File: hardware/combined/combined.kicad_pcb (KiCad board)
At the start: 2 copper layers, 62 x 208.5 mm, 143 parts, among them J1 USB-C 5V in, J2 Mini-DIN-8 to printer, J4 Mini-DIN-8 LocalTalk, SW1 EVQP44B3M, SW2 B3U-1000P, SW3 TS-1002-BR16026, U1 ESP32-S3-WROOM-1-N8R2, U2 SP3490EN-L, U3 SP3232EEN, U4 AP7361C-33E, U5 USBLC6-2SC6, U6 SP3485EN-L, U7 PIC12F1840-I/P, U8 SP3485EN-L, U9 74AHCT1G125SE-7

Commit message: SW1: redraw EVQP44B3M footprint from Panasonic ANCTB27E, move to the east edge
The old footprint was an admitted estimate: four pads at (+-2.55, +-1.0). The real
part has two contacts at +-2.275 mm, 2.05-3.1 mm from the board edge, and two
anchor tabs at +-3.2 mm, 0.45-1.25 mm from the edge. Each contact fell between
two old pads and each tab overlapped one, so EN would have bonded to a frame tab.
New footprint traced from the drawing (tabs un-netted); SW1 placed so the push
plate is flush with x=162; EN rerouted; GND via added. DRC 0/0 with parity.
Combined file, fab package and render regenerated.
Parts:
- moved SW1 2.33 mm to (160.3, 99.5)
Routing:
- net /EN: track 56.1 -> 57.7 mm
- net /GND: track 0.00 -> 1.40 mm, vias 43 -> 44

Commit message: LEDs: drop the pad-1 silk labels; keep Wells's inboard SW1 position; antenna copper stays
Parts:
- moved SW1 3.05 mm to (157.2, 99.5)
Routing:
- net /EN: track 57.7 -> 52.4 mm
- net /GND: track 1.40 -> 0.00 mm

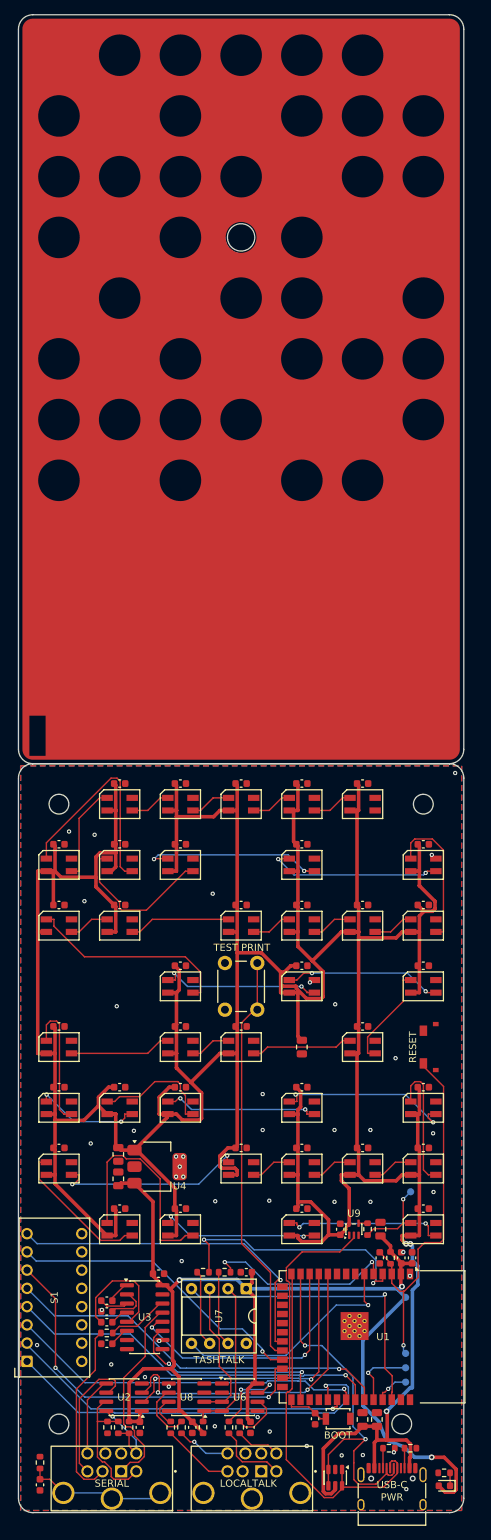
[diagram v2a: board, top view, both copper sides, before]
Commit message: Panel: plate the test hole — gold to the bore, no black surround
The 3.8mm test hole becomes a plated pad (O4.4 pad, copper layers only):
the bore wall takes ENIG and reads gold, the keep_dia black surround and
its sub-0.1mm mask sliver are gone, and mask opens to the drill edge.
Pad + annulus ring + tab art share decorative net PANEL_AU so their
contact doesn't DRC as a short; combine_boards.py carries that one net
through and strips all others (a pad's stripped (net 0) doesn't parse -
delete the node instead). Flood window grown to clear the pad by 0.25mm.
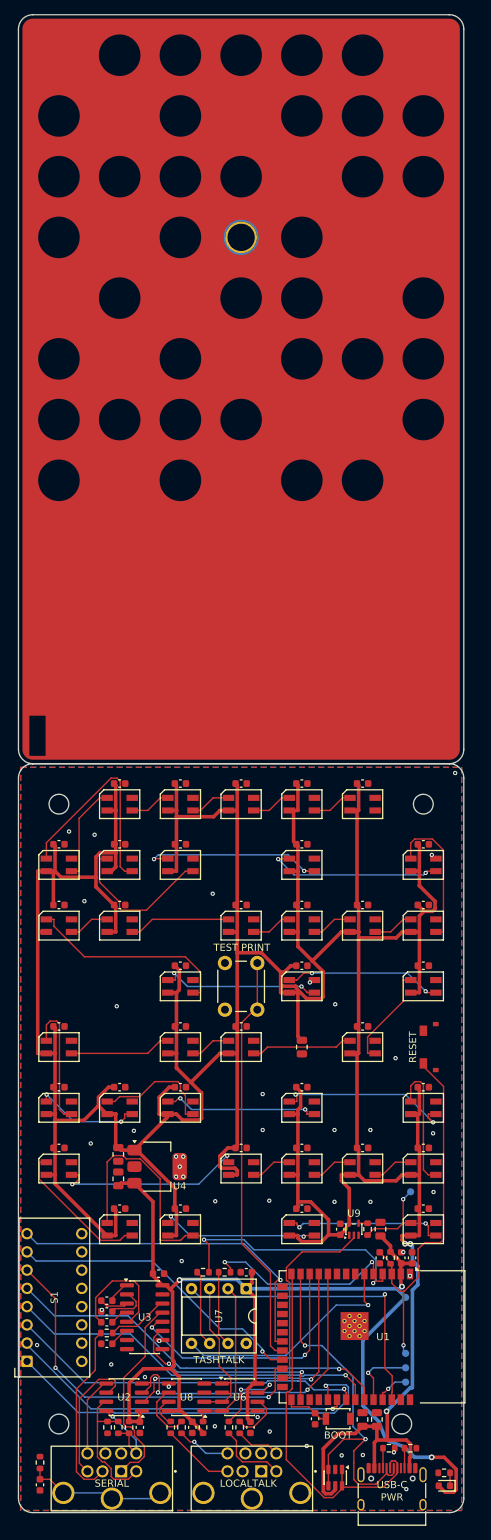
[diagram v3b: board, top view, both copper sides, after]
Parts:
- moved MT3 100.1 mm to (156.4, 47.7)
- moved MT4 98.6 mm to (108.6, 47.7)
- moved MT2 86.3 mm to (105.6, -38.6)
- moved MT1 86.3 mm to (156.4, -38.6)
- renumbered MT3 to MT1, MT4 to MT2, MT2 to MT3, MT1 to MT4
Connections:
- H_TEST pad : (no net) -> PANEL_AU

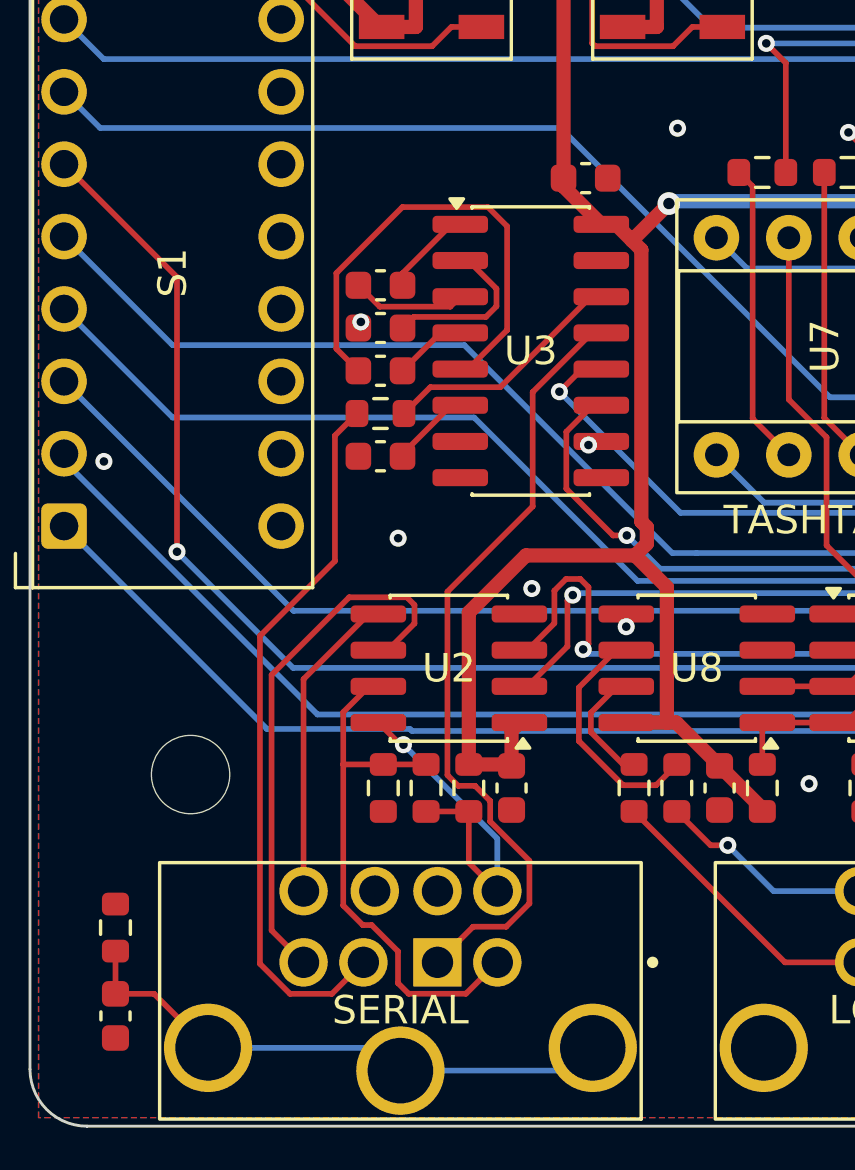
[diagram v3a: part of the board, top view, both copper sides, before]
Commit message: Review #4 fixes: J2 flipped to Mac-style, THT thermal reliefs, D3 restocked part, order notes corrected
Fourth adversarial pre-order review (layout, LCSC parts, circuit); report in
docs/review-2026-09-01-pre-order-4.md. No dead-on-arrival defect found; these are the
fixes it produced:

- J2 (printer port) is now wired as a Macintosh serial port so Apple's own crossover
  cable (590-0552-A / M0197) is the right cable. Schematic labels swapped 1<->2, 3<->5,
  6<->8; six nets hand re-routed (three new signal vias, one GND stitch via at
  111.45,152.6); DNP resistors R5 and R7 rotated 180 deg to suit the new pin map.
  J2 and J4 now read the same way.
- Both /GND zones use THT thermal reliefs (were solid; J2/J4 are hand-soldered).
  The change stranded one island, re-tied by tools_pcb/r12_fix.py with a via at
  119.626,131.048. GND is one cluster, 153/153 pads.
- D3 is LCSC C12624 (KT-0603G); C72043 had one unit in stock.
- ORDER-NOTES: 0.12 mm (4.7 mil) space exception around U4's tab (the .kicad_dru
  always required it), corrected via-fill answer (13 vias touch SMD pads, four fully
  inside U3.10/C9.2/C12.2/U1.1), D3 part, and the printer-cable guidance.
- Combined package regenerated (pos 127 rows, drill floor 0.30, 3.8 mm PTH, seam
  copper >= 0.5 mm) and the assembly render refreshed.
- Docs: SPEC 2.4 rewritten for the Mac-style J2 and the cable; HANDOFF entry with the
  bring-up traps (LT_DE floats as shipped, IO35/T1IN float, never ICSP the PIC in the
  socket, IO48 brownout loop) and drift corrections (LED caps at 2.87 mm, SW1 on the
  east edge, H4 coordinates, J4 shell direct to GND); firmware audit corrected on IO35.

Verification: ERC 0 errors; source DRC --severity-all --schematic-parity
--refill-zones = 0 errors / 0 unconnected (5 lib notes, 80 field-parity notes);
combined-file DRC baseline unchanged apart from one benign starved_thermal on U7.8.
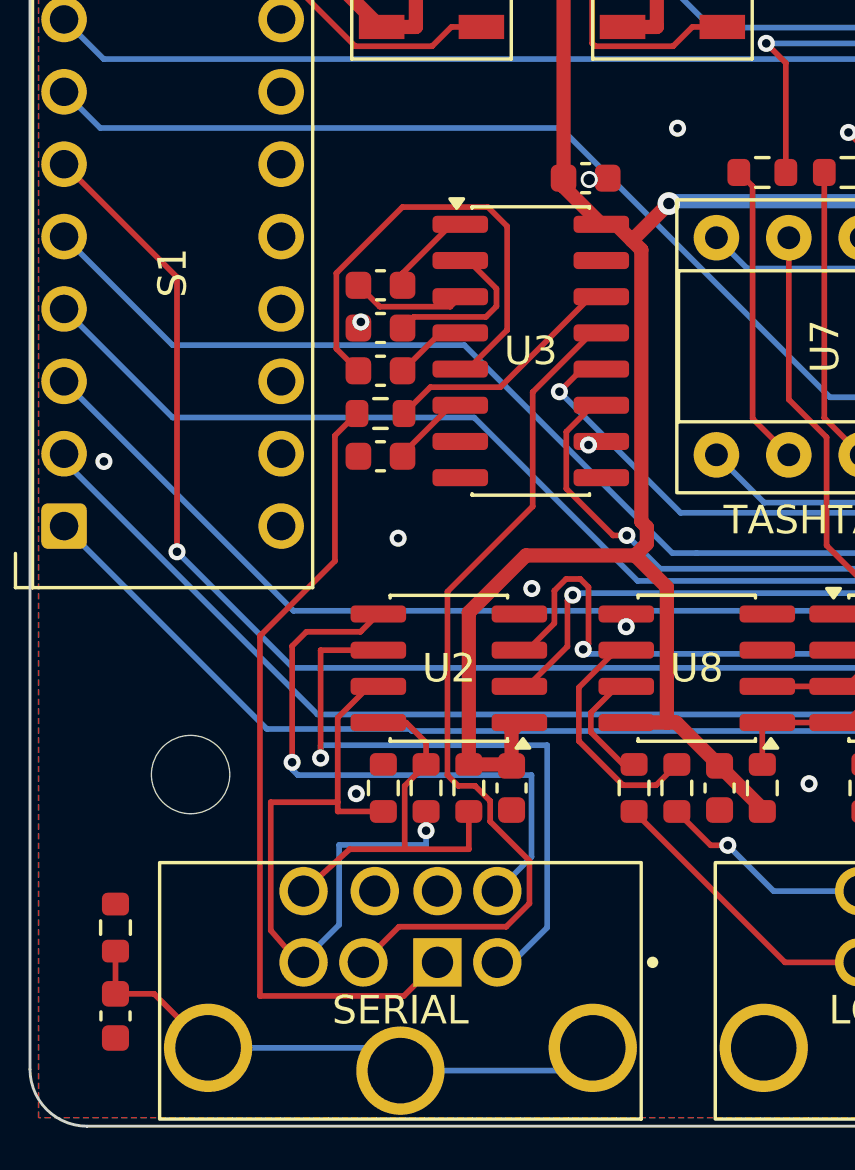
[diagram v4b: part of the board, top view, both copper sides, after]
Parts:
- turned R5 to -90 degrees
- turned R7 to 90 degrees
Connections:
- J2 pad 1: /PR_HSKO -> /PR_HSKI
- J2 pad 2: /PR_HSKI -> /PR_HSKO
- J2 pad 3: /PR_TXD_N -> /PR_RXD_N
- J2 pad 5: /PR_RXD_N -> /PR_TXD_N
- J2 pad 6: /PR_TXD_P -> /PR_RXD_P
- J2 pad 8: /PR_RXD_P -> /PR_TXD_P
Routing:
- net /PR_RXD_P: track 11.0 -> 20.9 mm, vias 0 -> 1
- net /PR_TXD_N: track 19.1 -> 24.1 mm, vias 0 -> 1
- net /PR_RXD_N: track 19.1 -> 22.9 mm, vias 0 -> 1
- net /PR_HSKI: track 25.2 -> 28.6 mm
- net /PR_HSKO: track 28.1 -> 30.7 mm
- net /PR_TXD_P: track 12.4 -> 13.7 mm, vias 1 -> 0
- net /GND: vias 44 -> 46

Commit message: Panel: swap too-small test label for a dot mark (PCBWay EQ)
PCBWay flagged the "test" soldermask label on the cover panel as below
their minimum feature size. Frame 9 drops that four-glyph label and adds a
~0.9mm accent dot in the test cell's lobe, with the lobe corner radius
opened from 10u to 12u.

The dot is emitted as a #111111 mask-knockout path -- the panel pipeline
ignores <circle> and only ingests white/#fff/#111 fills, so a plain black
circle would have been silently dropped. As a knockout it renders as a
kept-soldermask island on exposed gold. Regenerated panel -> combined ->
fab. Smallest B_Mask features in that cell: 0.90mm island, 0.23mm opening.
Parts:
- moved MT2 100.1 mm to (105.6, -38.6)
- moved MT3 100.1 mm to (156.4, 47.7)
- renumbered MT3 to MT2, MT2 to MT3

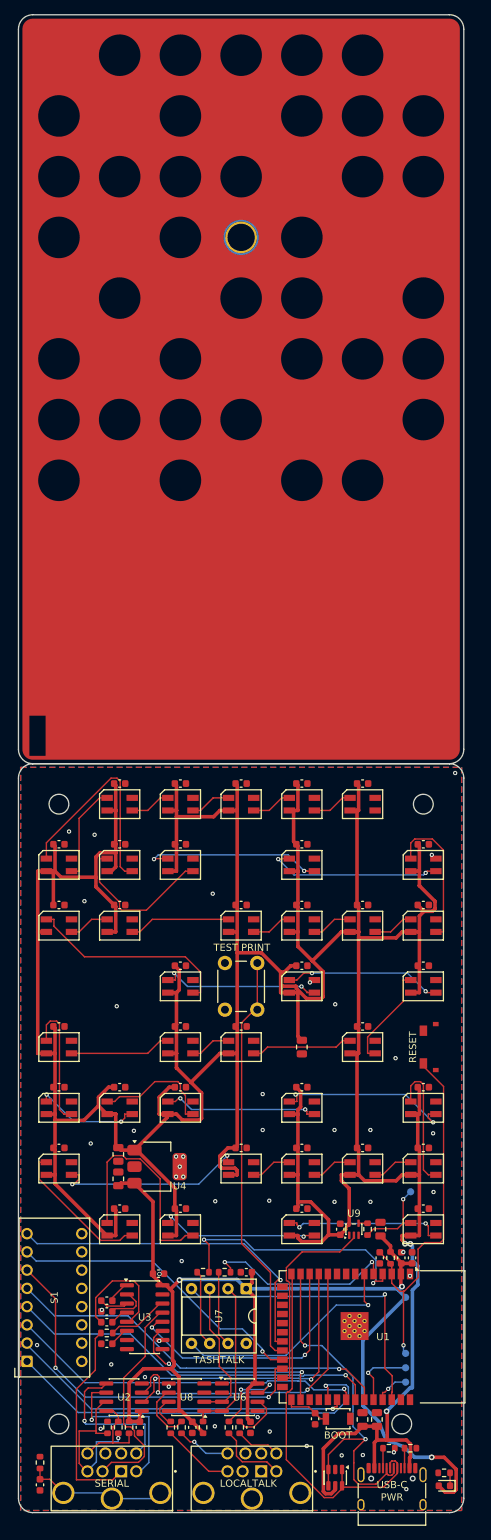
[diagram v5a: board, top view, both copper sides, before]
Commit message: Fab package: regenerated from the routed rev 2026.11 board (W-1091)
138 placements on AirWriter, 61 on Lite; drill floor 0.30 mm. The combined
panel's DRC under its default rules shows only the known kinds; R17 and D3 add
one copper-edge and one silk-edge item each way, both clear under the main
board's own 0.25 mm edge rule.
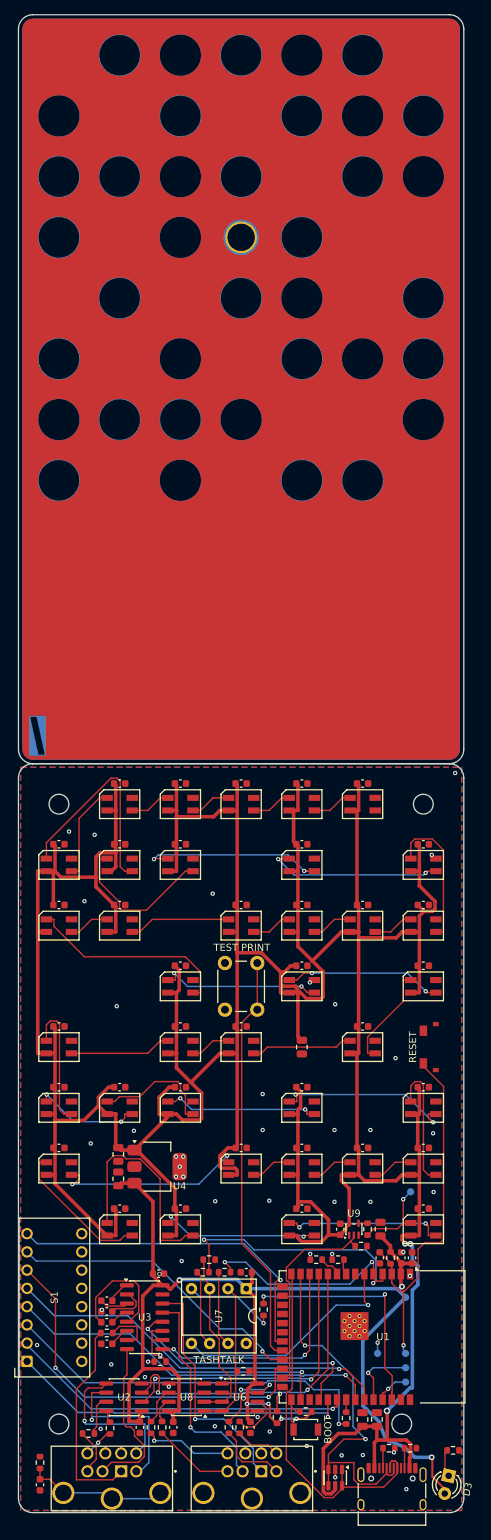
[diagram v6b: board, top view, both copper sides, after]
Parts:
- removed C7: 100n, Capacitor_SMD:C_0603_1608Metric
- removed R5: 120R, Resistor_SMD:R_0603_1608Metric
- removed R6, R7: 4.7k, Resistor_SMD:R_0603_1608Metric
- added R21: 10k, Resistor_SMD:R_0603_1608Metric, F.Cu at (140.0, 150.2)
- added R22: 10k, Resistor_SMD:R_0603_1608Metric, F.Cu at (126.5, 129.1)
- added R23: 10k, Resistor_SMD:R_0603_1608Metric, F.Cu at (147.7, 127.2)
- added R24: 10k, Resistor_SMD:R_0603_1608Metric, F.Cu at (119.7, 143.2)
- added R25: 10k, Resistor_SMD:R_0603_1608Metric, F.Cu at (136.0, 151.0)
- added R27: 1k, Resistor_SMD:R_0603_1608Metric, F.Cu at (134.1, 136.0)
- added R28: 1k, Resistor_SMD:R_0603_1608Metric, F.Cu at (145.6, 151.1)
- added R29: 10k, Resistor_SMD:R_0603_1608Metric, F.Cu at (112.8, 152.5)
- added R30: 10k, Resistor_SMD:R_0603_1608Metric, F.Cu at (109.8, 153.2)
- added R32: 10k, Resistor_SMD:R_0603_1608Metric, F.Cu at (141.4, 129.1)
- added R33: 10k, Resistor_SMD:R_0603_1608Metric, F.Cu at (144.5, 129.1)
- added TP9: GND, TestPoint_Pad_D1.0mm, B.Cu at (150.0, 142.1)
- D3: footprint LED_SMD:LED_0603_1608Metric -> airwriter:LED_D3.0mm_Spacer_H8mm
- R17: value 1k -> 150R
- SW3: value TS-1002-BR16026 -> TS-1002-BR15026
- U3: value SP3232EEN -> SP3232EBEN-L/TR
- U9: value 74AHCT1G125SE-7 -> SN74LV1T125DCKR
- moved R14 9.60 mm to (131.3, 144.6), turned to 180 degrees
- moved SW2 4.74 mm to (140.0, 152.7)
- moved R11 4.25 mm to (118.5, 152.4)
- moved R17 3.37 mm to (160.5, 155.6), turned to 0 degrees
- moved C18 2.65 mm to (121.5, 152.4)
- moved D3 1.51 mm to (159.9, 159.1), turned to -102.5 degrees
- moved R10 1.20 mm to (120.0, 152.4)
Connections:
- net /LT_A renamed /LT_RXD_N
- net /LT_B renamed /LT_RXD_P
- net /LT_PORT_A renamed /LT_PORT_RXD_N
- net /LT_PORT_B renamed /LT_PORT_RXD_P
- net /LT_PORT_Y renamed /LT_PORT_TXD_N
- net /LT_PORT_Z renamed /LT_PORT_TXD_P
- net /LT_Y renamed /LT_TXD_N
- net /LT_Z renamed /LT_TXD_P
- J4 pad 1: unconnected-(J4-HSKo-Pad1) -> /J4_HSKO
- J4 pad 2: unconnected-(J4-HSKi-Pad2) -> /J4_HSKI
- U1 pad 30: unconnected-(U1-IO37-Pad30) -> /J4_HSKI_RX
- U1 pad 33: /DIP3 -> /DIP3_GPIO
- U1 pad 8: unconnected-(U1-IO15-Pad8) -> /BOARD_LITE
- U1 pad 9: unconnected-(U1-IO16-Pad9) -> /BOARD_REV
- U2 pad 7: /PR_TXD_N -> /PR_TXD_N_IN
- U2 pad 8: /PR_TXD_P -> /PR_TXD_P_IN
- U3 pad 10: /GND -> /HSKI_DRV
- U3 pad 12: /UART_CTS -> /J4_HSKI_RX
- U3 pad 13: /PR_HSKO -> /J4_HSKI
- U3 pad 14: /HSKI_RS232 -> /J4_HSKO
- U3 pad 7: unconnected-(U3-T2OUT-Pad7) -> /HSKI_RS232
- U3 pad 8: /GND -> /PR_HSKO
- U3 pad 9: unconnected-(U3-R2OUT-Pad9) -> /UART_CTS
- U7 pad 4: /LT_RESET -> /LT_MCLR
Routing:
- net /J4_HSKI_RX: track 0.00 -> 35.4 mm, vias 0 -> 2
- net /J4_HSKO: track 0.00 -> 33.1 mm, vias 0 -> 1
- net /J4_HSKI: track 0.00 -> 30.2 mm, vias 0 -> 1
- net /PR_TXD_N: track 24.1 -> 6.47 mm, vias 1 -> 0
- net /LT_MCLR: track 0.00 -> 13.1 mm, vias 0 -> 1
- net /LT_RESET: track 42.6 -> 33.1 mm, vias 1 -> 2
- net /PR_TXD_P: track 13.7 -> 4.26 mm, vias 0 -> 1
- net /DIP1: track 55.6 -> 47.8 mm
- net /+3V3: track 166.7 -> 174.3 mm, vias 3 -> 7
- net /PR_HSKO: track 30.7 -> 23.4 mm
- net /PR_TXD_N_IN: track 0.00 -> 5.60 mm
- net /GND: track 0.00 -> 5.04 mm, vias 46 -> 50
- net /LT_PORT_RXD_P: track 7.56 -> 12.1 mm
- net /UART_CTS: track 36.6 -> 32.1 mm
- net /LT_DE: track 20.1 -> 24.4 mm
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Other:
- board text added: "AirWriter rev 2026.11"
- board text added: "CERN-OHL-S-2.0"
- board text added: "github.com/wr/airwriter"
- board text removed: "PWR"

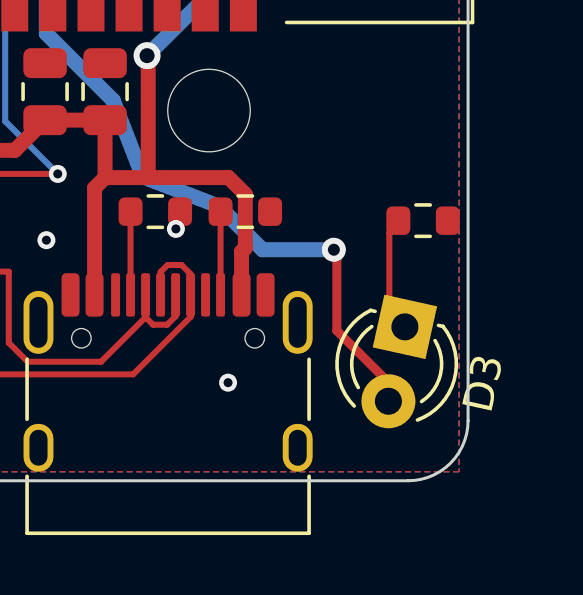
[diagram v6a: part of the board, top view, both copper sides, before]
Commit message: Rev 2026.11: fixes from the board review (W-1091)
- R17 moves 0.3 mm west: its ground pad sat 0.275 mm from the routed edge,
  under PCBWay's 0.30 minimum with a +-0.2 mm router.
- D3's cathode gets a K on the silk past pad 1, where the spacer doesn't
  hide it; its designator goes to F.Fab, as rev A's LEDs, off the edge.
- R29/R30 go from 10 k to 15 k: against U2's typical 15 k input, 10 k let
  a -15 V RS-232 line reach -9 V, past the SP3490's -7 V common mode.
- The order notes ask to keep J4's holes free of solder, and add
  airwriter-top.png, the main board at ~40 px/mm, for polarity checks.
- r13_check.py checks pad-to-edge, silk on the board and D3's mark.

Refs: W-1091
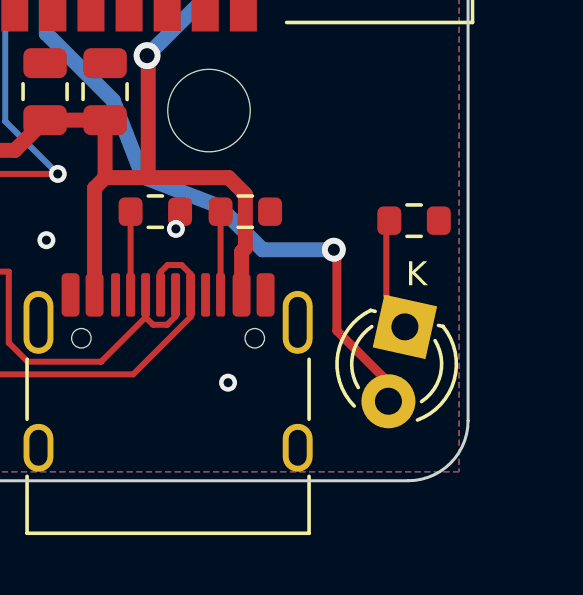
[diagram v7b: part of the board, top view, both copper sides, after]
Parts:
- R29, R30: value 10k -> 15k
- moved R17 0.30 mm to (160.2, 155.6)
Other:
- board text added: "K"
